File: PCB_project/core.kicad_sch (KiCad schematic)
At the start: 31 parts, among them SW1 SW_Push, U1 HPM5301IEGx, X1 24MHz

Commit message: PCB layout 完毕
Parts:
- removed C2: 0.1uF, Capacitor_SMD:C_0402_1005Metric, symbol Device:C
- added R10, R11: 33Ω, Resistor_SMD:R_0402_1005Metric, symbol Device:R
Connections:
- net JTAG_TDI: now also RN2.5 (R4.2); no longer RN2.8 (R1.2)
- net JTAG_TDO: now also RN2.6 (R3.2); no longer RN2.7 (R2.2)
- net SPI_CS: now also U1.25 (PB10/TMR0.COMP2/URT2.DE/URT2.RTS/SPI2.CS0/ACMP.COMP0/USB0.PWR/ADC0.IN2/CMP0.INP4/CMP1.INP4), U1.42 (PA26/SPI1.CS0/XPI0.CA_D3/TRGM0.P02); no longer RN1.8 (R1.2), RN2.5 (R4.2)
- net SWCLK/JTAG_TCK: now also RN2.7 (R2.2); no longer RN2.6 (R3.2)
- net uart_rx: now also R11.1; no longer U1.11 (PA01/TMR1.CAPT0/URT0.RXD/TRGM0.P01/ACMP.COMP0)
- net uart_tx: now also R10.1; no longer U1.12 (PA00/TMR1.COMP0/URT0.TXD/TRGM0.P00)
- net at RN1.1 (R1.1): no longer U1.42 (PA26/SPI1.CS0/XPI0.CA_D3/TRGM0.P02)
- net at RN2.1 (R1.1): no longer U1.22 (PB13/TMR1.COMP3/URT3.DE/URT3.RTS/I2C3.SCL/SPI2.MOSI/TRGM0.P01/ADC0.IN5/CMP0.INP2/CMP1.INP2)
- net at RN2.2 (R2.1): now also U1.24 (PB11/URT2.CTS/SPI2.SCLK/ACMP.COMP1/ADC0.IN3/CMP0.INN4/CMP1.INN4); no longer U1.23 (PB12/URT3.CTS/I2C3.SDA/SPI2.MISO/TRGM0.P00/ADC0.IN4/CMP0.INN2/CMP1.INN2)
- net at RN2.3 (R3.1): now also U1.23 (PB12/URT3.CTS/I2C3.SDA/SPI2.MISO/TRGM0.P00/ADC0.IN4/CMP0.INN2/CMP1.INN2); no longer U1.24 (PB11/URT2.CTS/SPI2.SCLK/ACMP.COMP1/ADC0.IN3/CMP0.INN4/CMP1.INN4)
- net at RN2.4 (R4.1): now also U1.22 (PB13/TMR1.COMP3/URT3.DE/URT3.RTS/I2C3.SCL/SPI2.MOSI/TRGM0.P01/ADC0.IN5/CMP0.INP2/CMP1.INP2); no longer U1.25 (PB10/TMR0.COMP2/URT2.DE/URT2.RTS/SPI2.CS0/ACMP.COMP0/USB0.PWR/ADC0.IN2/CMP0.INP4/CMP1.INP4)
- net LED: now reaches U1.48 (PA05/TMR1.COMP2/URT1.DE/URT1.RTS/SPI0.SCLK/TRGM0.P05/JTAG.TDI)
- new net: R10.2, U1.12 (PA00/TMR1.COMP0/URT0.TXD/TRGM0.P00)
- new net: R11.2, U1.11 (PA01/TMR1.CAPT0/URT0.RXD/TRGM0.P01/ACMP.COMP0)
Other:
- moved on the sheet: C22, C23, C24, R4, R5, RN1, SW1, U1D

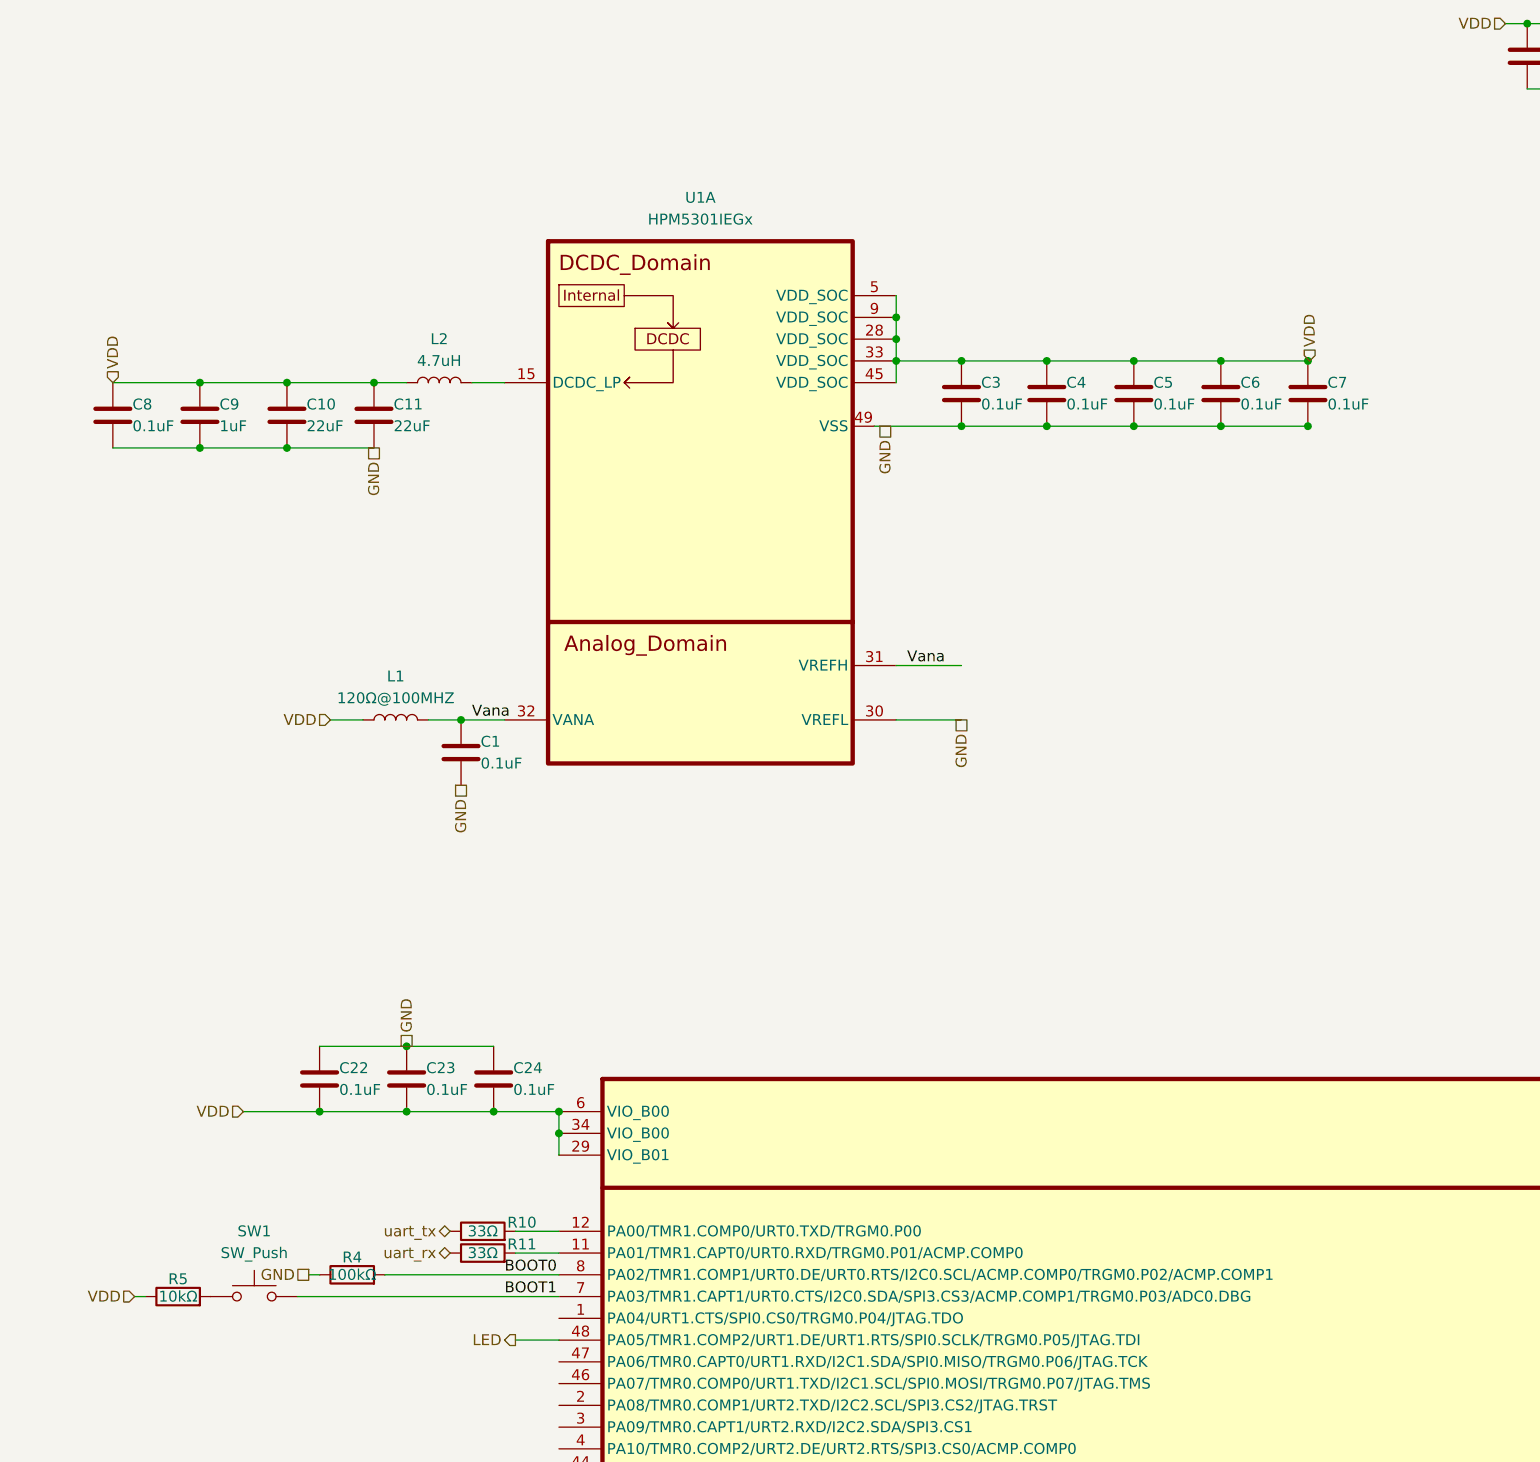
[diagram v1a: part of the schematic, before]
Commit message: 原理图错误，HPM5301的VDD_SOC引脚应当连接到内部DCDC_LP(输出)，不应当连接到3.3V供电
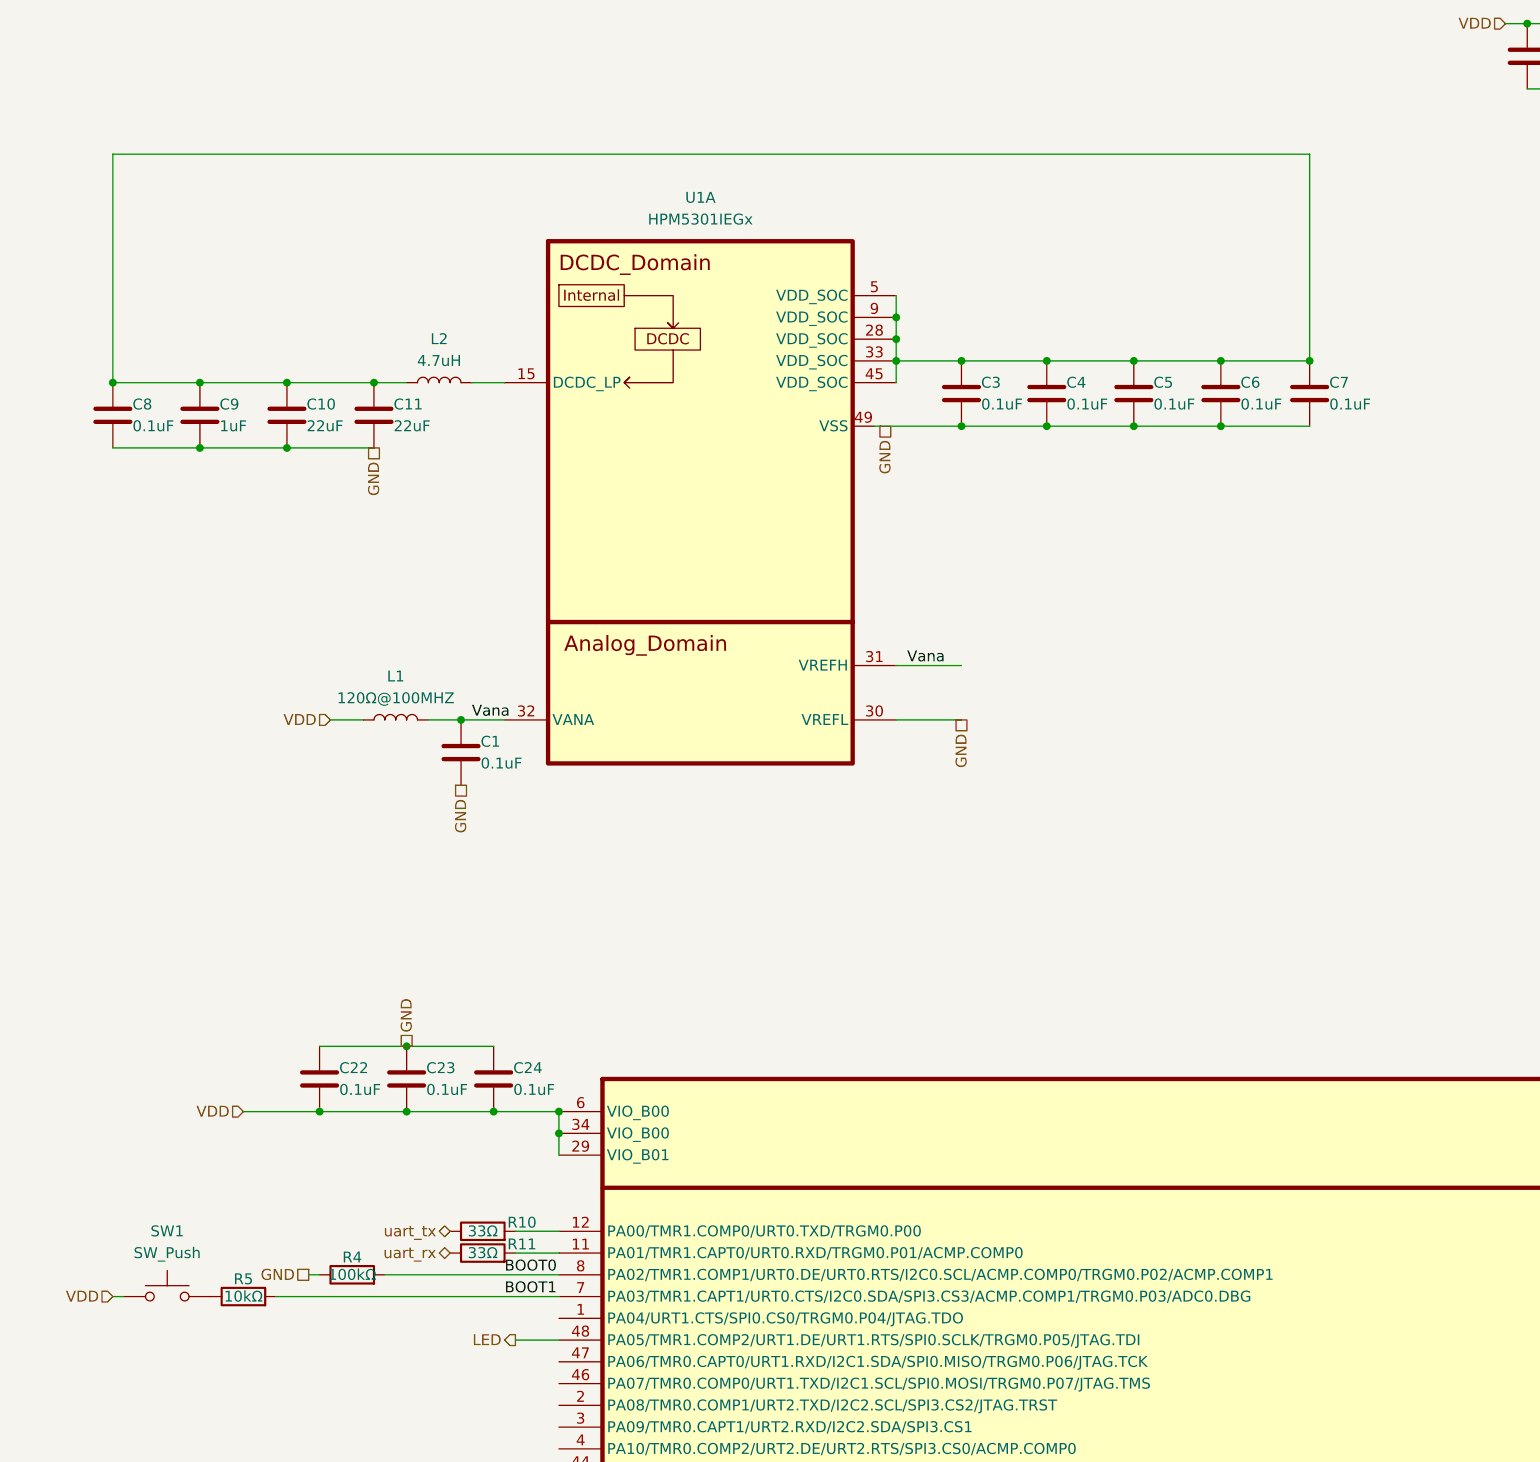
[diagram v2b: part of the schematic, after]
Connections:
- net BOOT1: now also R5.2; no longer SW1.2
- net VDD: now also SW1.1; no longer C10.1, C11.1, C3.1, C4.1, C5.1, C6.1, C7.1, C8.1, C9.1, L2.1, R5.1, U1.28 (VDD_SOC), U1.33 (VDD_SOC), U1.45 (VDD_SOC), U1.5 (VDD_SOC), U1.9 (VDD_SOC)
- new net: C10.1, C11.1, C3.1, C4.1, C5.1, C6.1, C7.1, C8.1, C9.1, L2.1, U1.28 (VDD_SOC), U1.33 (VDD_SOC), U1.45 (VDD_SOC), U1.5 (VDD_SOC), U1.9 (VDD_SOC)
- new net: R5.1, SW1.2
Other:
- moved on the sheet: SW1
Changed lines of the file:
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@@
 	)
 	(junction
-		(at 91.44 168.91)
+		(at 39.37 81.28)
 		(diameter 0)
 		(color 0 0 0 0)
 	)
 	(junction
-		(at 148.3881 78.74)
+		(at 91.44 168.91)
 		(diameter 0)
 		(color 0 0 0 0)
 	)
 	(junction
-		(at 80.01 120.65)
+		(at 148.3881 78.74)
 		(diameter 0)
 		(color 0 0 0 0)
 	)
 	(junction
-		(at 178.8681 78.74)
+		(at 80.01 120.65)
 		(diameter 0)
 		(color 0 0 0 0)
@@
 	)
 	(junction
-		(at 178.8681 86.36)
+		(at 179.07 78.74)
 		(diameter 0)
 		(color 0 0 0 0)
@@
 	(wire
 		(pts
-			(xy 41.91 187.96) (xy 43.18 187.96)
+			(xy 39.37 187.96) (xy 40.64 187.96)
 		)
 		(stroke
@@
 	(wire
 		(pts
-			(xy 60.96 187.96) (xy 91.44 187.96)
-		)
-		(stroke
-			(width 0)
-			(type default)
-		)
-	)
-	(wire
-		(pts
 			(xy 130.81 114.3) (xy 138.43 114.3)
 		)
@@
 	(wire
 		(pts
-			(xy 168.7081 86.36) (xy 178.8681 86.36)
+			(xy 168.7081 86.36) (xy 179.07 86.36)
 		)
 		(stroke
@@
 	(wire
 		(pts
-			(xy 178.8681 78.74) (xy 179.07 78.74)
+			(xy 168.7081 78.74) (xy 179.07 78.74)
 		)
 		(stroke
@@
 	(wire
 		(pts
-			(xy 178.8681 86.36) (xy 179.07 86.36)
-		)
-		(stroke
-			(width 0)
-			(type default)
-		)
-	)
-	(wire
-		(pts
 			(xy 39.37 88.9) (xy 49.53 88.9)
 		)
@@
 	(wire
 		(pts
+			(xy 39.37 81.28) (xy 39.37 54.61)
+		)
+		(stroke
+			(width 0)
+			(type default)
+		)
+	)
+	(wire
+		(pts
 			(xy 370.84 48.26) (xy 381 48.26)
 		)
@@
 	(wire
 		(pts
-			(xy 130.81 78.74) (xy 130.81 81.28)
+			(xy 39.37 54.61) (xy 179.07 54.61)
 		)
 		(stroke
@@
 	(wire
 		(pts
-			(xy 138.43 86.36) (xy 148.3881 86.36)
+			(xy 130.81 78.74) (xy 130.81 81.28)
 		)
 		(stroke
@@
 	(wire
 		(pts
-			(xy 71.12 223.52) (xy 68.58 223.52)
+			(xy 138.43 86.36) (xy 148.3881 86.36)
 		)
 		(stroke
@@
 	(wire
 		(pts
-			(xy 168.7081 78.74) (xy 178.8681 78.74)
+			(xy 71.12 223.52) (xy 68.58 223.52)
 		)
 		(stroke
@@
 	(wire
 		(pts
+			(xy 58.42 187.96) (xy 91.44 187.96)
+		)
+		(stroke
+			(width 0)
+			(type default)
+		)
+	)
+	(wire
+		(pts
 			(xy 78.74 242.57) (xy 91.44 242.57)
 		)
@@
 	(wire
 		(pts
+			(xy 179.07 54.61) (xy 179.07 78.74)
+		)
+		(stroke
+			(width 0)
+			(type default)
+		)
+	)
+	(wire
+		(pts
 			(xy 91.44 168.91) (xy 91.44 171.45)
 		)
@@
 	(hierarchical_label "VDD"
 		(shape input)
-		(at 41.91 187.96 180)
+		(at 39.37 187.96 180)
 		(fields_autoplaced yes)
 		(effects
@@
 		)
 	)
-	(hierarchical_label "VDD"
-		(shape input)
-		(at 179.07 78.74 90)
-		(fields_autoplaced yes)
-		(effects
-			(font
-				(size 1.27 1.27)
-			)
-			(justify left)
-		)
-	)
 	(hierarchical_label "uart_tx"
 		(shape bidirectional)
@@
 		)
 	)
-	(hierarchical_label "VDD"
-		(shape input)
-		(at 39.37 81.28 90)
-		(fields_autoplaced yes)
-		(effects
-			(font
-				(size 1.27 1.27)
-			)
-			(justify left)
-		)
-	)
 	(hierarchical_label "USB_D-"
 		(shape input)
@@
 		)
 		(instances
-			(project ""
+			(project "hpm_dap"
 				(path "/159ca461-ea29-45ac-b98a-f1d5e536ce91/d4d51e8b-0106-4120-b0f8-2449cdfd6410"
 					(reference "R1")
@@
 	(symbol
 		(lib_id "Device:C")
-		(at 178.8681 82.55 0)
+		(at 179.07 82.55 0)
 		(unit 1)
 		(exclude_from_sim no)
@@
 		(dnp no)
 		(property "Reference" "C7"
-			(at 181.1541 81.28 0)
+			(at 181.356 81.28 0)
 			(effects
 				(font
@@
 		)
 		(property "Value" "0.1uF"
-			(at 181.1541 83.82 0)
+			(at 181.356 83.82 0)
 			(effects
 				(font
@@
 		)
 		(property "Footprint" "Capacitor_SMD:C_0402_1005Metric"
-			(at 179.8333 86.36 0)
+			(at 180.0352 86.36 0)
 			(effects
 				(font
@@
 		)
 		(property "Datasheet" "~"
-			(at 178.8681 82.55 0)
+			(at 179.07 82.55 0)
 			(effects
 				(font
@@
 		)
 		(property "Description" "Unpolarized capacitor"
-			(at 178.8681 82.55 0)
+			(at 179.07 82.55 0)
 			(effects
 				(font
@@
 	(symbol
 		(lib_id "Switch:SW_Push")
-		(at 55.88 187.96 0)
+		(at 45.72 187.96 0)
 		(unit 1)
 		(exclude_from_sim no)
@@
 		(fields_autoplaced yes)
 		(property "Reference" "SW1"
-			(at 55.88 180.34 0)
+			(at 45.72 180.34 0)
 			(effects
 				(font
@@
 		)
 		(property "Value" "SW_Push"
-			(at 55.88 182.88 0)
+			(at 45.72 182.88 0)
 			(effects
 				(font
@@
 		)
 		(property "Footprint" "Button_Switch_SMD:SW_Push_SPST_NO_Alps_SKRK"
-			(at 55.88 182.88 0)
+			(at 45.72 182.88 0)
 			(effects
 				(font
@@
 		)
 		(property "Datasheet" "~"
-			(at 55.88 182.88 0)
+			(at 45.72 182.88 0)
 			(effects
 				(font
@@
 		)
 		(property "Description" "Push button switch, generic, two pins"
-			(at 55.88 187.96 0)
+			(at 45.72 187.96 0)
 			(effects
 				(font
@@
 		)
 		(instances
-			(project ""
+			(project "hpm_dap"
 				(path "/159ca461-ea29-45ac-b98a-f1d5e536ce91/d4d51e8b-0106-4120-b0f8-2449cdfd6410"
 					(reference "SW1")
@@
 		)
 		(instances
-			(project ""
+			(project "hpm_dap"
 				(path "/159ca461-ea29-45ac-b98a-f1d5e536ce91/d4d51e8b-0106-4120-b0f8-2449cdfd6410"
 					(reference "C1")
@@
 		)
 		(instances
-			(project ""
-				(path "/159ca461-ea29-45ac-b98a-f1d5e536ce91/d4d51e8b-0106-4120-b0f8-2449cdfd6410"
-					(reference "L1")
-					(unit 1)
-				)
-			)
-		)
-	)
-	(symbol
-		(lib_id "Device:R")
-		(at 46.99 187.96 90)
-		(unit 1)
-		(exclude_from_sim no)
-		(in_bom yes)
-		(on_board yes)
-		(dnp no)
-		(property "Reference" "R5"
-			(at 46.99 185.928 90)
-			(effects
-				(font
-					(size 1.27 1.27)
-				)
-			)
-		)
-		(property "Value" "10kΩ"
-			(at 46.99 187.96 90)
-			(effects
-				(font
-					(size 1.27 1.27)
-				)
-			)
-		)
-		(property "Footprint" "Resistor_SMD:R_0402_1005Metric"
-			(at 46.99 189.738 90)
-			(effects
-				(font
-					(size 1.27 1.27)
-				)
-				(hide yes)
-			)
-		)
-		(property "Datasheet" "~"
-			(at 46.99 187.96 0)
-			(effects
-				(font
-					(size 1.27 1.27)
-				)
-				(hide yes)
-			)
-		)
-		(property "Description" "Resistor"
-			(at 46.99 187.96 0)
-			(effects
-				(font
-					(size 1.27 1.27)
-				)
-				(hide yes)
-			)
-		)
-		(pin "1"
-		)
-		(pin "2"
-		)
-		(instances
 			(project "hpm_dap"
 				(path "/159ca461-ea29-45ac-b98a-f1d5e536ce91/d4d51e8b-0106-4120-b0f8-2449cdfd6410"
-					(reference "R5")
+					(reference "L1")
 					(unit 1)
 				)
@@
 		)
 		(instances
-			(project ""
+			(project "hpm_dap"
 				(path "/159ca461-ea29-45ac-b98a-f1d5e536ce91/d4d51e8b-0106-4120-b0f8-2449cdfd6410"
 					(reference "L2")
@@
 					(unit 1)
 				)
+			)
+		)
+	)
+	(symbol
+		(lib_id "Device:R")
+		(at 54.61 187.96 90)
+		(unit 1)
+		(exclude_from_sim no)
+		(in_bom yes)
+		(on_board yes)
+		(dnp no)
+		(property "Reference" "R5"
+			(at 54.61 185.928 90)
+			(effects
+				(font
+					(size 1.27 1.27)
+				)
+			)
+		)
+		(property "Value" "10kΩ"
+			(at 54.61 187.96 90)
+			(effects
+				(font
+					(size 1.27 1.27)
+				)
+			)
+		)
+		(property "Footprint" "Resistor_SMD:R_0402_1005Metric"
+			(at 54.61 189.738 90)
+			(effects
+				(font
+					(size 1.27 1.27)
+				)
+				(hide yes)
+			)
+		)
+		(property "Datasheet" "~"
+			(at 54.61 187.96 0)
+			(effects
+				(font
+					(size 1.27 1.27)
+				)
+				(hide yes)
+			)
+		)
+		(property "Description" "Resistor"
+			(at 54.61 187.96 0)
+			(effects
+				(font
+					(size 1.27 1.27)
+				)
+				(hide yes)
+			)
+		)
+		(pin "1"
+		)
+		(pin "2"
+		)
+		(instances
+			(project "hpm_dap"
+				(path "/159ca461-ea29-45ac-b98a-f1d5e536ce91/d4d51e8b-0106-4120-b0f8-2449cdfd6410"
+					(reference "R5")
+					(unit 1)
+				)
